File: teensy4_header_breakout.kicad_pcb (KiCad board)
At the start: 2 copper layers, 22.9 x 35.6 mm, 3 parts, among them J1 Conn_01x14, J2 Conn_01x14, U1 GND-1

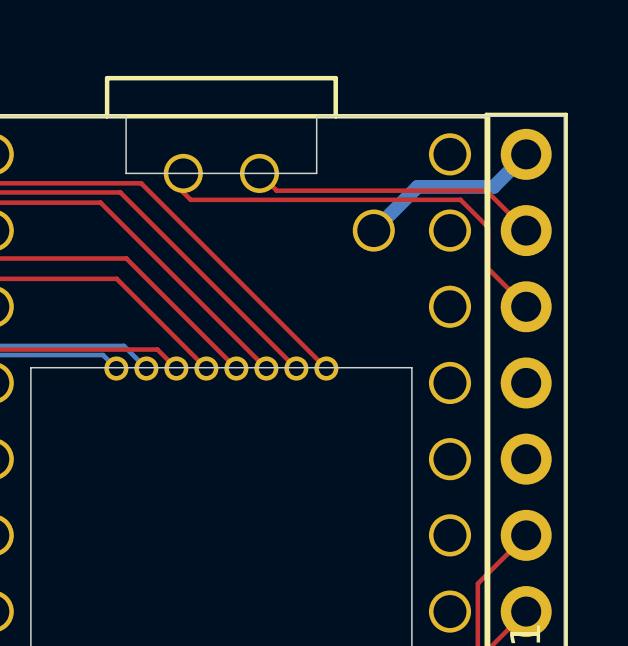
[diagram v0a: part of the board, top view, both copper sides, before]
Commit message: Updated two unused pins to GND to allow a basic USB cable to be attached.
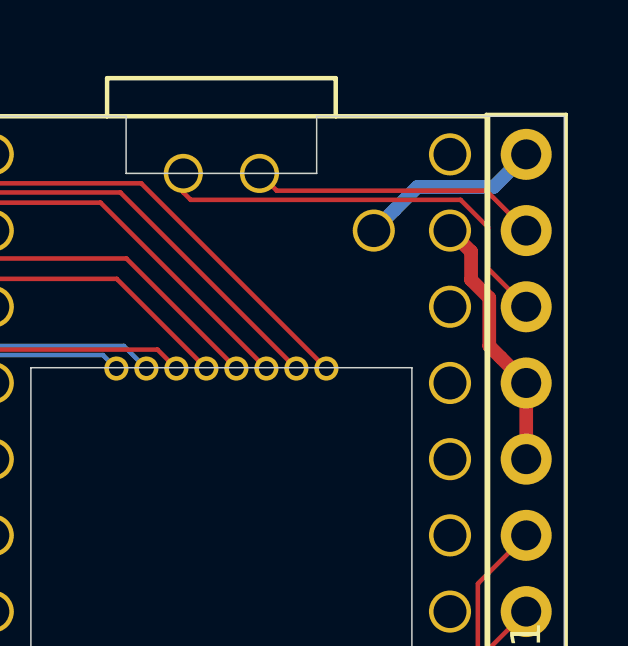
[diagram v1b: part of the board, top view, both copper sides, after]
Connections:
- J2 pad 10: (no net) -> /GND
- J2 pad 11: (no net) -> /GND
- U1 pad 32: (no net) -> /GND
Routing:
- net /GND: track 0.00 -> 8.67 mm
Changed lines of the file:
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@@
-(kicad_pcb (version 20171130) (host pcbnew "(5.1.2-1)-1")
+(kicad_pcb (version 20171130) (host pcbnew "(5.1.4-0-10_14)")
   (general
     (thickness 1.6)
     (drawings 35)
-    (tracks 125)
+    (tracks 133)
     (zones 0)
     (modules 3)
-    (nets 27)
+    (nets 28)
   )
   (page A4)
@@
   )
   (setup
-    (last_trace_width 0.1524)
+    (last_trace_width 0.4572)
     (user_trace_width 0.1524)
     (user_trace_width 0.3048)
@@
   (net 25 /GND-1)
   (net 26 /3V3-1)
+  (net 27 /GND)
   (net_class Default "This is the default net class."
     (clearance 0.1524)
@@
     (add_net /DAT2)
     (add_net /DAT3)
+    (add_net /GND)
     (add_net /GND-1)
     (add_net /GND-SD)
@@
     (add_net /VBAT)
     (add_net /VUSB)
+    (add_net "Net-(U1-Pad1)")
+    (add_net "Net-(U1-Pad10)")
+    (add_net "Net-(U1-Pad11)")
+    (add_net "Net-(U1-Pad12)")
+    (add_net "Net-(U1-Pad13)")
+    (add_net "Net-(U1-Pad14)")
+    (add_net "Net-(U1-Pad2)")
+    (add_net "Net-(U1-Pad20)")
+    (add_net "Net-(U1-Pad21)")
+    (add_net "Net-(U1-Pad22)")
+    (add_net "Net-(U1-Pad23)")
+    (add_net "Net-(U1-Pad24)")
+    (add_net "Net-(U1-Pad25)")
+    (add_net "Net-(U1-Pad26)")
+    (add_net "Net-(U1-Pad27)")
+    (add_net "Net-(U1-Pad28)")
+    (add_net "Net-(U1-Pad29)")
+    (add_net "Net-(U1-Pad3)")
+    (add_net "Net-(U1-Pad30)")
+    (add_net "Net-(U1-Pad31)")
+    (add_net "Net-(U1-Pad33)")
+    (add_net "Net-(U1-Pad4)")
+    (add_net "Net-(U1-Pad5)")
+    (add_net "Net-(U1-Pad6)")
+    (add_net "Net-(U1-Pad7)")
+    (add_net "Net-(U1-Pad8)")
+    (add_net "Net-(U1-Pad9)")
   )
   (net_class Power ""
@@
     (pad 34 thru_hole circle (at -13.97 -5.08 270) (size 1.404 1.404) (drill 1.1) (layers *.Cu *.Mask)
       (net 15 /VUSB))
-    (pad 32 thru_hole circle (at -13.97 -7.62 270) (size 1.404 1.404) (drill 1.1) (layers *.Cu *.Mask))
+    (pad 32 thru_hole circle (at -13.97 -7.62 270) (size 1.404 1.404) (drill 1.1) (layers *.Cu *.Mask)
+      (net 27 /GND))
     (pad 31 thru_hole circle (at -11.43 -7.62 270) (size 1.404 1.404) (drill 1.1) (layers *.Cu *.Mask))
     (pad 30 thru_hole circle (at -8.89 -7.62 270) (size 1.404 1.404) (drill 1.1) (layers *.Cu *.Mask))
@@
     (pad 12 thru_hole oval (at 0 27.94 180) (size 1.7 1.7) (drill 1) (layers *.Cu *.Mask)
       (net 17 /D+))
-    (pad 11 thru_hole oval (at 0 25.4 180) (size 1.7 1.7) (drill 1) (layers *.Cu *.Mask))
-    (pad 10 thru_hole oval (at 0 22.86 180) (size 1.7 1.7) (drill 1) (layers *.Cu *.Mask))
+    (pad 11 thru_hole oval (at 0 25.4 180) (size 1.7 1.7) (drill 1) (layers *.Cu *.Mask)
+      (net 27 /GND))
+    (pad 10 thru_hole oval (at 0 22.86 180) (size 1.7 1.7) (drill 1) (layers *.Cu *.Mask)
+      (net 27 /GND))
     (pad 9 thru_hole oval (at 0 20.32 180) (size 1.7 1.7) (drill 1) (layers *.Cu *.Mask)
       (net 19 /27))
@@
   (segment (start 149.86 99.06) (end 151.469399 97.450601) (width 0.1524) (layer B.Cu) (net 14) (status 10))
   (segment (start 151.469399 88.453311) (end 151.953311 87.969399) (width 0.1524) (layer B.Cu) (net 14))
-  (segment (start 166.556999 82.363001) (end 165.1 83.82) (width 0.4572) (layer B.Cu) (net 15) (status 20))
+  (segment (start 165.801999 83.118001) (end 165.1 83.82) (width 0.4572) (layer B.Cu) (net 15))
+  (segment (start 166.556999 82.363001) (end 165.801999 83.118001) (width 0.4572) (layer B.Cu) (net 15))
   (segment (start 169.096999 82.363001) (end 166.556999 82.363001) (width 0.4572) (layer B.Cu) (net 15))
-  (segment (start 170.18 81.28) (end 169.096999 82.363001) (width 0.4572) (layer B.Cu) (net 15) (status 10))
+  (segment (start 170.18 81.28) (end 169.096999 82.363001) (width 0.4572) (layer B.Cu) (net 15))
   (segment (start 170.18 83.82) (end 168.85079 82.49079) (width 0.1524) (layer F.Cu) (net 16) (status 10))
   (segment (start 168.85079 82.49079) (end 161.86579 82.49079) (width 0.1524) (layer F.Cu) (net 16))
@@
   (segment (start 169.330001 107.529999) (end 169.330001 108.248117) (width 0.4572) (layer F.Cu) (net 26))
   (segment (start 158.936999 112.843001) (end 157.88601 113.89399) (width 0.4572) (layer F.Cu) (net 26))
+  (segment (start 168.948999 87.668999) (end 169.330001 88.050001) (width 0.4572) (layer F.Cu) (net 27))
+  (segment (start 168.948999 86.066157) (end 168.948999 87.668999) (width 0.4572) (layer F.Cu) (net 27))
+  (segment (start 168.341999 85.459157) (end 168.948999 86.066157) (width 0.4572) (layer F.Cu) (net 27))
+  (segment (start 169.330001 88.050001) (end 170.18 88.9) (width 0.4572) (layer F.Cu) (net 27))
+  (segment (start 168.341999 84.521999) (end 168.341999 85.459157) (width 0.4572) (layer F.Cu) (net 27))
+  (segment (start 167.64 83.82) (end 168.341999 84.521999) (width 0.4572) (layer F.Cu) (net 27))
+  (segment (start 170.18 88.9) (end 170.18 91.44) (width 0.4572) (layer F.Cu) (net 27))
 )

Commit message: Update date on silkscreen
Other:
- board text added: "2019-09-19"
- board text removed: "2019-09-10"
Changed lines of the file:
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@@
   )
   (setup
-    (last_trace_width 0.4572)
+    (last_trace_width 0.1524)
     (user_trace_width 0.1524)
     (user_trace_width 0.3048)
@@
     (add_net /VBAT)
     (add_net /VUSB)
-    (add_net "Net-(U1-Pad1)")
-    (add_net "Net-(U1-Pad10)")
-    (add_net "Net-(U1-Pad11)")
-    (add_net "Net-(U1-Pad12)")
-    (add_net "Net-(U1-Pad13)")
-    (add_net "Net-(U1-Pad14)")
-    (add_net "Net-(U1-Pad2)")
-    (add_net "Net-(U1-Pad20)")
-    (add_net "Net-(U1-Pad21)")
-    (add_net "Net-(U1-Pad22)")
-    (add_net "Net-(U1-Pad23)")
-    (add_net "Net-(U1-Pad24)")
-    (add_net "Net-(U1-Pad25)")
-    (add_net "Net-(U1-Pad26)")
-    (add_net "Net-(U1-Pad27)")
-    (add_net "Net-(U1-Pad28)")
-    (add_net "Net-(U1-Pad29)")
-    (add_net "Net-(U1-Pad3)")
-    (add_net "Net-(U1-Pad30)")
-    (add_net "Net-(U1-Pad31)")
-    (add_net "Net-(U1-Pad33)")
-    (add_net "Net-(U1-Pad4)")
-    (add_net "Net-(U1-Pad5)")
-    (add_net "Net-(U1-Pad6)")
-    (add_net "Net-(U1-Pad7)")
-    (add_net "Net-(U1-Pad8)")
-    (add_net "Net-(U1-Pad9)")
   )
   (net_class Power ""
@@
   (gr_circle (center 161.29 81.915) (end 161.671 82.931) (layer B.SilkS) (width 0.12))
   (gr_circle (center 165.1 83.82) (end 165.354 85.09) (layer B.SilkS) (width 0.12))
-  (gr_text 2019-09-10 (at 159.9438 111.6584) (layer B.SilkS)
+  (gr_text 2019-09-19 (at 159.9438 111.6584) (layer B.SilkS)
     (effects (font (size 1.27 1.27) (thickness 0.2032)) (justify mirror))
   )

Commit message: Generated gerbers for order to AllPCB
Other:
- board text added: "2019-10-03"
- board text removed: "2019-09-19"
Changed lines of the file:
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@@
   (general
     (thickness 1.6)
-    (drawings 35)
+    (drawings 36)
     (tracks 133)
     (zones 0)
@@
     )
   )
+  (gr_circle (center 167.64 83.82) (end 167.894 85.09) (layer B.SilkS) (width 0.12))
   (gr_circle (center 154.94 109.22) (end 155.321 110.363) (layer B.SilkS) (width 0.12))
   (gr_circle (center 157.48 109.22) (end 157.861 110.236) (layer B.SilkS) (width 0.12))
@@
   (gr_circle (center 161.29 81.915) (end 161.671 82.931) (layer B.SilkS) (width 0.12))
   (gr_circle (center 165.1 83.82) (end 165.354 85.09) (layer B.SilkS) (width 0.12))
-  (gr_text 2019-09-19 (at 159.9438 111.6584) (layer B.SilkS)
+  (gr_text 2019-10-03 (at 159.9438 111.6584) (layer B.SilkS)
     (effects (font (size 1.27 1.27) (thickness 0.2032)) (justify mirror))
   )

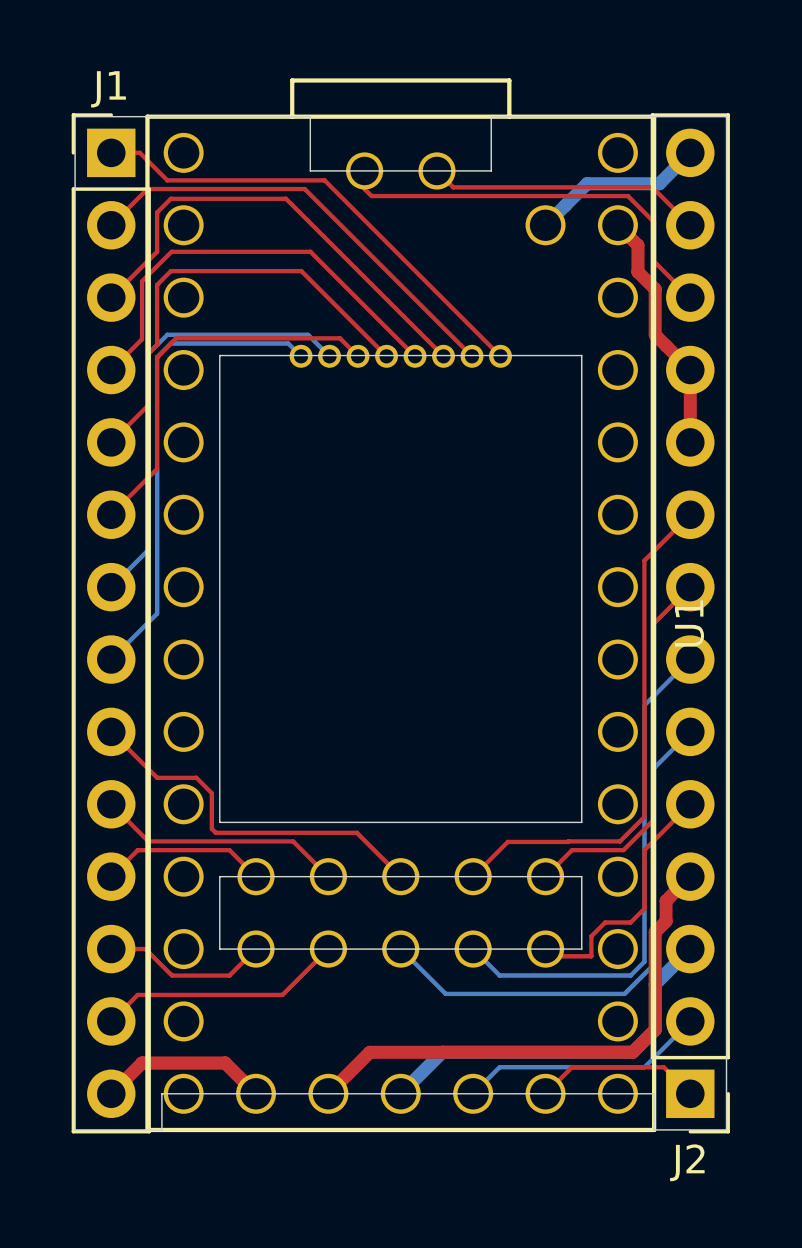
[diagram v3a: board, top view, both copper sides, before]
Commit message: Update board with new labels and square pads
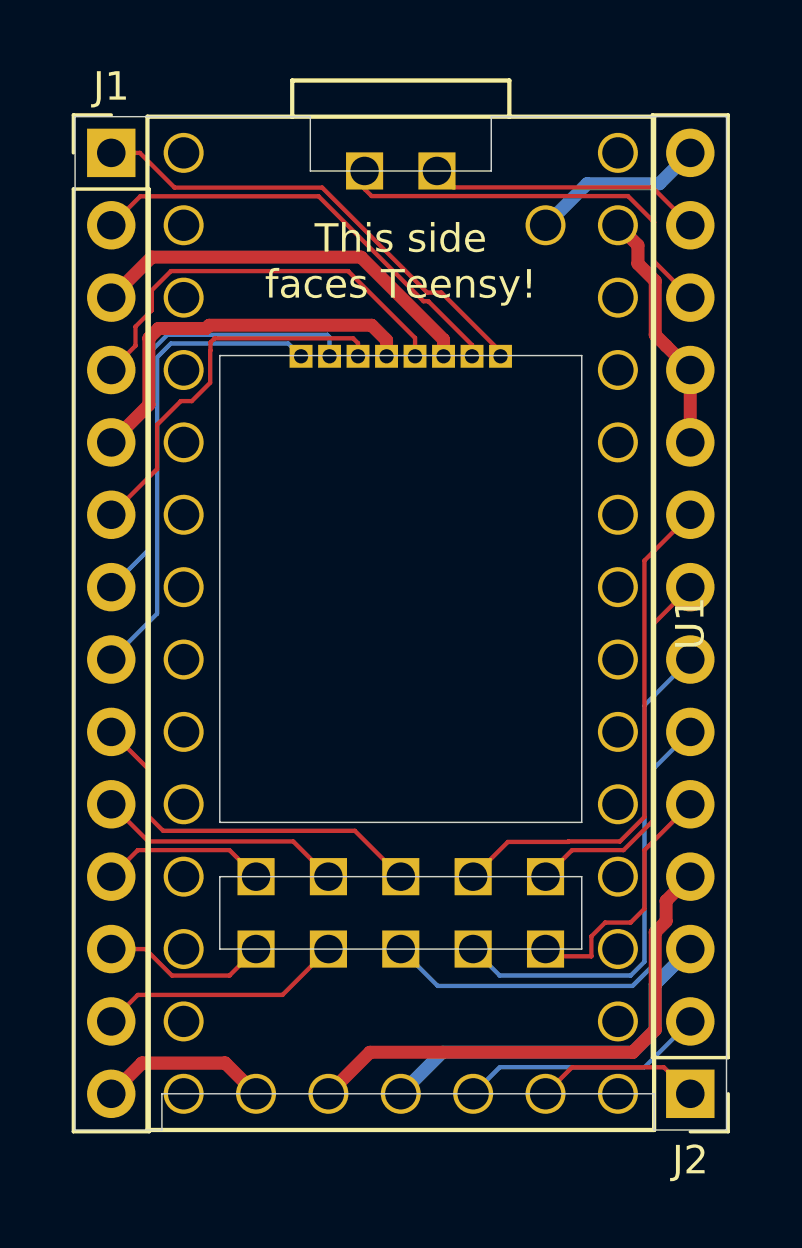
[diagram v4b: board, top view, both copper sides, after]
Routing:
- net /3V3-SD: track 15.3 -> 13.1 mm
- net /GND-SD: track 15.8 -> 13.7 mm
- net /DAT3: track 15.3 -> 15.8 mm
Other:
- board text added: "2019-10-11"
- board text added: "This side faces Teensy!"
- board text removed: "2019-10-03"

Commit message: Update readme, silkscreen and tweak outline
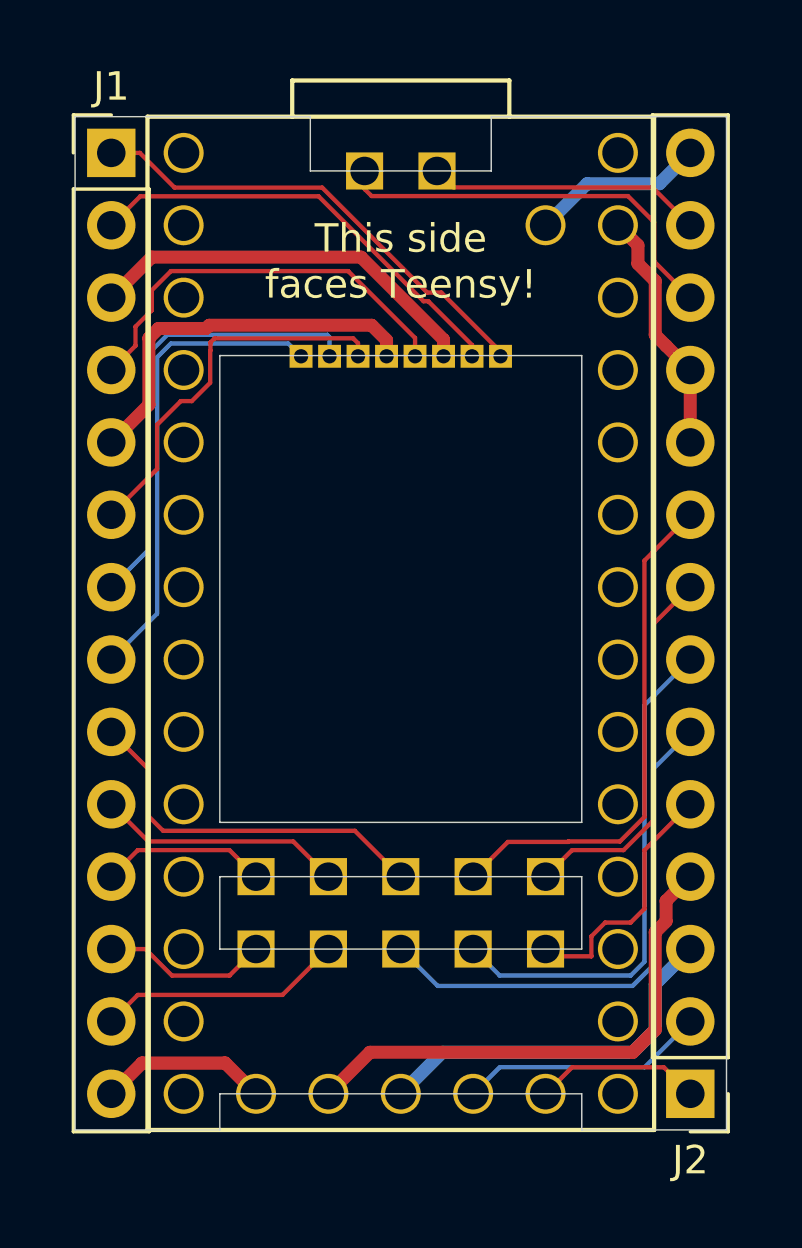
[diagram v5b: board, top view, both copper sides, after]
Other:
- outline, holes or cut-outs redrawn
- board text added: "2019-10-20"
- board text removed: "2019-10-11"
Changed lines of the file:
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@@
   (general
     (thickness 1.6)
-    (drawings 37)
+    (drawings 42)
     (tracks 148)
     (zones 0)
@@
   )
   (setup
-    (last_trace_width 0.1524)
+    (last_trace_width 0.4572)
     (user_trace_width 0.1524)
     (user_trace_width 0.3048)
@@
   (module Teensy:Teensy40_SMT (layer F.Cu)
     (at 160.02 97.79 270)
-    (fp_text reference U1 (at 0 -10.16 270) (layer F.SilkS)
+    (fp_text reference U1 (at 0 -10.16 270) (layer F.SilkS) hide
       (effects (font (size 1 1) (thickness 0.15)))
     )
@@
     )
   )
+  (gr_circle (center 165.1 114.3) (end 165.354 115.443) (layer B.SilkS) (width 0.12))
+  (gr_circle (center 162.56 114.3) (end 162.941 115.443) (layer B.SilkS) (width 0.12))
+  (gr_circle (center 160.02 114.3) (end 160.02 115.57) (layer B.SilkS) (width 0.12))
+  (gr_circle (center 157.48 114.3) (end 157.861 115.316) (layer B.SilkS) (width 0.12))
+  (gr_circle (center 154.94 114.3) (end 155.321 115.443) (layer B.SilkS) (width 0.12))
   (gr_text "This side\nfaces Teensy!" (at 160.02 85.09) (layer F.SilkS)
     (effects (font (size 1 1) (thickness 0.15)))
@@
   (gr_circle (center 161.29 81.915) (end 161.671 82.931) (layer B.SilkS) (width 0.12))
   (gr_circle (center 165.1 83.82) (end 165.354 85.09) (layer B.SilkS) (width 0.12))
-  (gr_text 2019-10-11 (at 159.9438 111.6584) (layer B.SilkS)
+  (gr_text 2019-10-20 (at 159.9438 111.6584) (layer B.SilkS)
     (effects (font (size 1.27 1.27) (thickness 0.2032)) (justify mirror))
   )
@@
     (effects (font (size 1.5 1.5) (thickness 0.3)) (justify mirror))
   )
-  (gr_line (start 151.638 115.57) (end 148.59 115.57) (layer Edge.Cuts) (width 0.05))
-  (gr_line (start 151.638 114.3) (end 151.638 115.57) (layer Edge.Cuts) (width 0.05))
-  (gr_line (start 168.91 114.3) (end 151.638 114.3) (layer Edge.Cuts) (width 0.05))
-  (gr_line (start 168.91 115.57) (end 168.91 114.3) (layer Edge.Cuts) (width 0.05))
-  (gr_line (start 171.45 115.57) (end 168.91 115.57) (layer Edge.Cuts) (width 0.05))
+  (gr_line (start 153.67 115.57) (end 148.59 115.57) (layer Edge.Cuts) (width 0.05))
+  (gr_line (start 153.67 114.3) (end 153.67 115.57) (layer Edge.Cuts) (width 0.05))
+  (gr_line (start 166.37 114.3) (end 153.67 114.3) (layer Edge.Cuts) (width 0.05))
+  (gr_line (start 166.37 115.57) (end 166.37 114.3) (layer Edge.Cuts) (width 0.05))
+  (gr_line (start 171.45 115.57) (end 166.37 115.57) (layer Edge.Cuts) (width 0.05))
   (gr_line (start 166.37 109.22) (end 166.37 106.68) (layer Edge.Cuts) (width 0.05))
   (gr_line (start 153.67 109.22) (end 166.37 109.22) (layer Edge.Cuts) (width 0.05))
@@
   (segment (start 160.985211 86.487011) (end 162.52 88.0218) (width 0.1524) (layer F.Cu) (net 8))
   (segment (start 149.86 86.36) (end 149.9108 86.36) (width 0.3048) (layer F.Cu) (net 9) (status 30))
-  (segment (start 161.52 87.8346) (end 161.52 87.98599) (width 0.4572) (layer F.Cu) (net 9))
   (segment (start 158.623 84.9376) (end 161.52 87.8346) (width 0.4572) (layer F.Cu) (net 9))
   (segment (start 151.2824 84.9376) (end 158.623 84.9376) (width 0.4572) (layer F.Cu) (net 9))
   (segment (start 149.86 86.36) (end 151.2824 84.9376) (width 0.4572) (layer F.Cu) (net 9))
+  (segment (start 161.52 87.8346) (end 161.52 88.4184) (width 0.4572) (layer F.Cu) (net 9))
   (segment (start 151.2824 86.805609) (end 151.2824 86.10031) (width 0.1524) (layer F.Cu) (net 10))
   (segment (start 151.953311 85.429399) (end 158.174999 85.429399) (width 0.1524) (layer F.Cu) (net 10))
@@
   (segment (start 158.174999 85.429399) (end 160.52 87.7744) (width 0.1524) (layer F.Cu) (net 10))
   (segment (start 150.709999 87.37801) (end 151.2824 86.805609) (width 0.1524) (layer F.Cu) (net 10))
+  (segment (start 153.297418 87.330589) (end 158.998611 87.330589) (width 0.4572) (layer F.Cu) (net 11))
   (segment (start 158.998611 87.330589) (end 159.52 87.851978) (width 0.4572) (layer F.Cu) (net 11))
-  (segment (start 159.52 87.851978) (end 159.52 87.98599) (width 0.4572) (layer F.Cu) (net 11))
-  (segment (start 153.297418 87.330589) (end 158.998611 87.330589) (width 0.4572) (layer F.Cu) (net 11))
-  (segment (start 153.185006 87.443001) (end 153.297418 87.330589) (width 0.4572) (layer F.Cu) (net 11))
-  (segment (start 149.86 91.44) (end 151.1808 90.1192) (width 0.4572) (layer F.Cu) (net 11))
-  (segment (start 151.1808 90.1192) (end 151.1808 87.7824) (width 0.4572) (layer F.Cu) (net 11))
   (segment (start 151.520199 87.443001) (end 153.185006 87.443001) (width 0.4572) (layer F.Cu) (net 11))
   (segment (start 151.1808 87.7824) (end 151.520199 87.443001) (width 0.4572) (layer F.Cu) (net 11))
+  (segment (start 153.185006 87.443001) (end 153.297418 87.330589) (width 0.4572) (layer F.Cu) (net 11))
+  (segment (start 151.1808 90.1192) (end 151.1808 87.7824) (width 0.4572) (layer F.Cu) (net 11))
+  (segment (start 149.86 91.44) (end 151.1808 90.1192) (width 0.4572) (layer F.Cu) (net 11))
+  (segment (start 159.52 87.851978) (end 159.52 88.4184) (width 0.4572) (layer F.Cu) (net 11))
   (segment (start 158.349 87.7878) (end 158.52 87.9588) (width 0.1524) (layer F.Cu) (net 12))
   (segment (start 153.3398 88.2142) (end 153.3398 87.9348) (width 0.1524) (layer F.Cu) (net 12))
